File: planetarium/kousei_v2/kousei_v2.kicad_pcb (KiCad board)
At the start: 2 copper layers, 94.5 x 66 mm, 44 parts, among them J13 Jack-DC, J2 Conn_01x03, J3 Conn_01x02, J4 Conn_01x02, J5 Conn_01x02, J6 Conn_01x02, J7 Conn_01x02, J8 Conn_01x02, U1 CL6808, U2 CL6808, U3 CL6808, U4 CL6808, U5 CL6808, U6 CL6808, U7 TC7WZ07FK, U8 R-78K5.0-2.0L

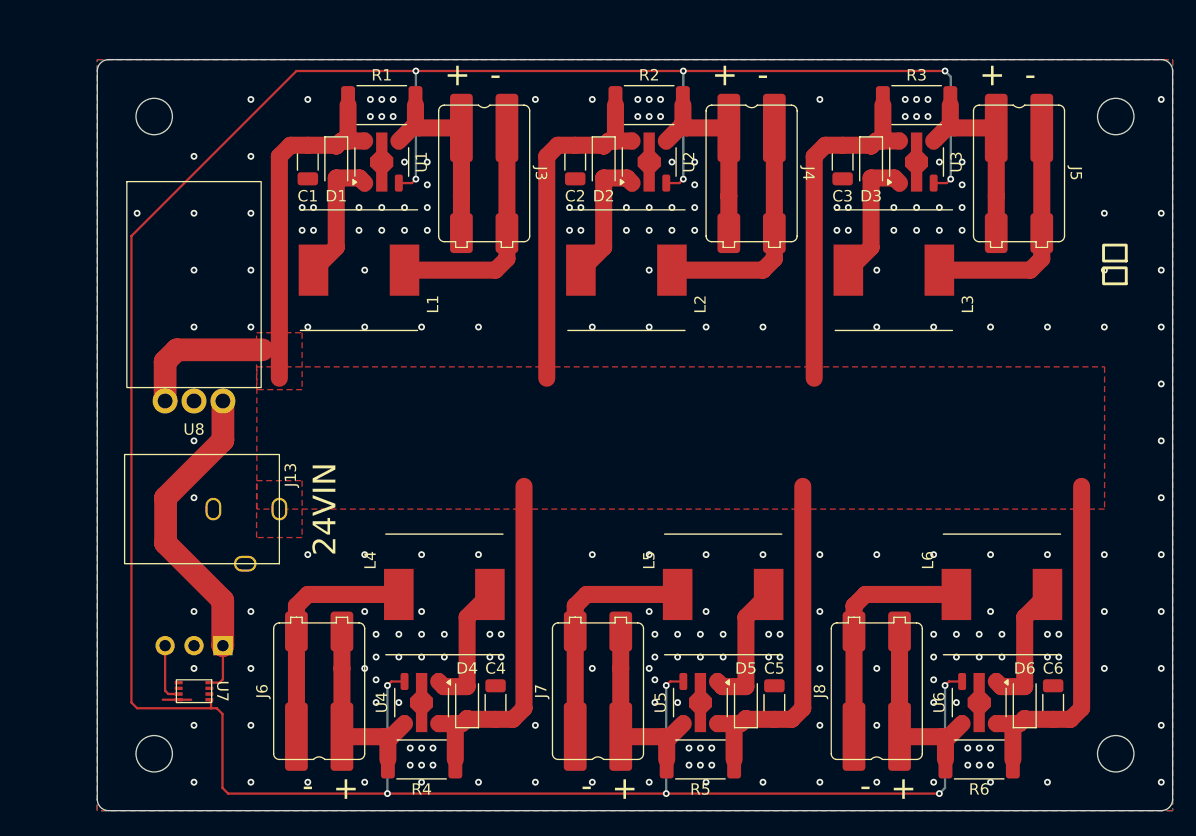
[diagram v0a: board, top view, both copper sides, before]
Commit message: change: LED追加, EN->nEN
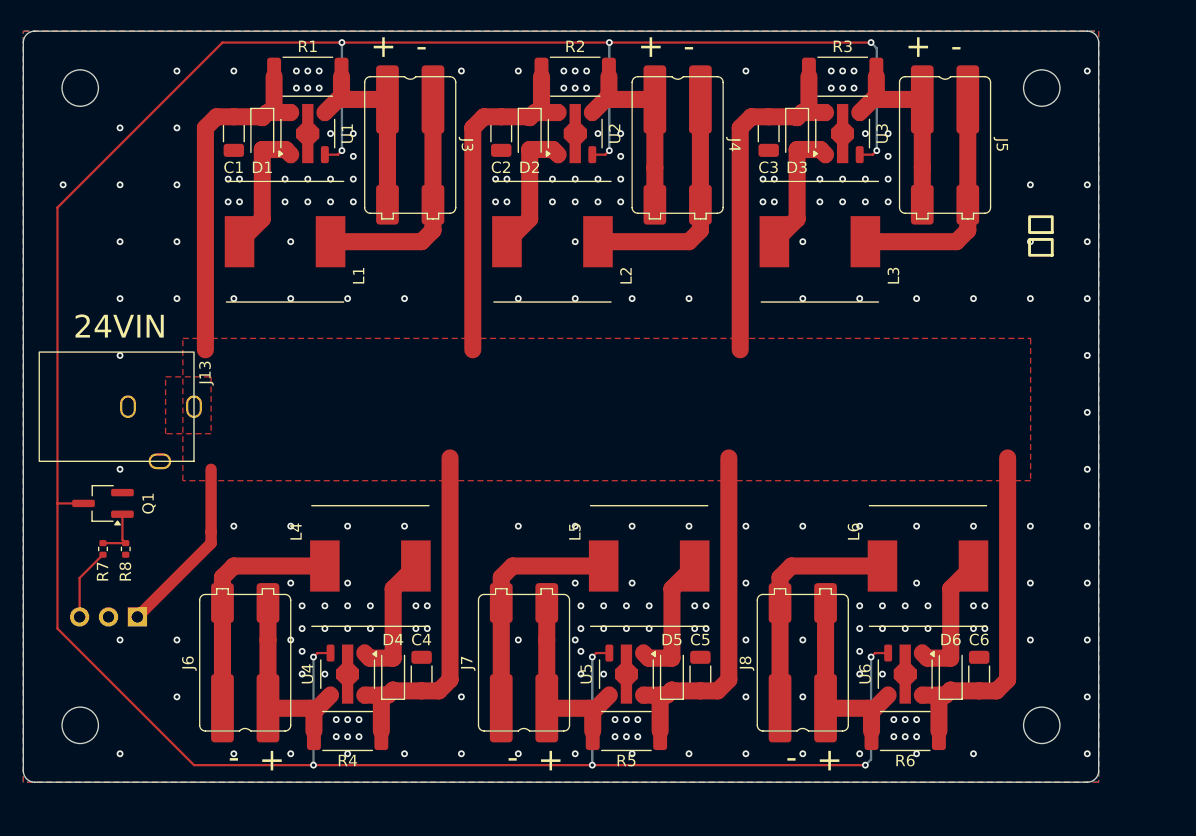
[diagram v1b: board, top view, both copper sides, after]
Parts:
- removed U7: TC7WZ07FK, TC7WZ07FK:TC7WZ07FK
- removed U8: R-78K5.0-2.0L, R-78K5.0-2.0L:R-78K5.0-2.0L
- added Q1: Q_NMOS, Package_TO_SOT_SMD:TSOT-23_HandSoldering, F.Cu at (107.0, 110.5)
- added R7: 100, Resistor_SMD:R_0402_1005Metric, F.Cu at (107.0, 114.5)
- added R8: 100k, Resistor_SMD:R_0402_1005Metric, F.Cu at (109.0, 114.5)
- moved J13 11.7 mm to (109.2, 102.0)
- moved J2 7.93 mm to (110.0, 120.5)
- moved C1 6.96 mm to (118.5, 78.0)
- moved C2 6.96 mm to (142.0, 78.0)
- moved C3 6.96 mm to (165.5, 78.0)
- moved C4 6.96 mm to (135.0, 125.5)
- moved C5 6.96 mm to (159.5, 125.5)
- moved C6 6.96 mm to (184.0, 125.5)
- moved D1 6.96 mm to (121.0, 78.0)
- moved D2 6.96 mm to (144.5, 78.0)
- moved D3 6.96 mm to (168.0, 78.0)
- moved D4 6.96 mm to (132.5, 125.5)
- moved D5 6.96 mm to (157.0, 125.5)
- moved D6 6.96 mm to (181.5, 125.5)
- moved J3 6.96 mm to (134.0, 79.0)
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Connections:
- J2 pad 1: +5V -> +24V
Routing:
- net +5V: track 29.9 -> 0.00 mm
- net ADJ: track 264.7 -> 260.1 mm
- net Net-(Q1-G): track 0.00 -> 4.66 mm
- net +24V: track 197.2 -> 200.4 mm
- net GND: track 2.50 -> 0.00 mm, vias 224 -> 220
- net EN: track 5.27 -> 6.32 mm
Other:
- board text added: "24VOUT"
- board text removed: "5VOUT"
